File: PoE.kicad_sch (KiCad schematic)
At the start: 86 parts, among them Q2 BSZ440N10NS3GATMA1, Q3 MMBTA06, T1 PA2467NL, U23 MP8008, U24 TCMT1107, U28 TCMT1107, U29 TL431DBZ

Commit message: Weeded out all ERC errors
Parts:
- removed C95: 220u/25V, Capacitor_Tantalum_SMD:CP_EIA-7343-31_Kemet-D, symbol Device:CP_Small
- added R903: 51R, Resistor_SMD:R_0402_1005Metric, symbol Device:R_Small
- added R906: 75R, Resistor_SMD:R_0402_1005Metric, symbol Device:R_Small
- added R916, R917: 24k, Resistor_SMD:R_0805_2012Metric, symbol Device:R_Small
- C901: renamed from C75; value 220n/50V -> 220nF/50V; LCSC (none) -> C5378
- C902: renamed from C16; value 10n/100V -> 10nF/100V; LCSC (none) -> C24944
- C903: renamed from C83; value 10n/100V -> 10nF/100V; LCSC (none) -> C24944
- C904: renamed from C110; value 10n/100V -> 10nF/100V; LCSC (none) -> C24944
- C905: renamed from C74; value 10n/100V -> 10nF/100V; LCSC (none) -> C24944
- C906: renamed from C76; value 1n/100V -> 1nF/100V; LCSC (none) -> C28233
- C907: renamed from C73; value 4u7/16V -> 4.7uF/16V; LCSC (none) -> C1779
- C908: renamed from C89; value 2u2/100V -> 2.2uF/100V; LCSC (none) -> C7393990
- C909: renamed from C79; value 100n/100V -> 100nF/100V; LCSC (none) -> C28233
- C910: renamed from C82; value 100n/100V -> 100nF/100V; LCSC (none) -> C28233
- C911: renamed from C84; value 100n/100V -> 100nF/100V; LCSC (none) -> C28233
- C912: renamed from C85; value 47u/63V -> 47uF/63V; symbol Device:CP_Small -> Device:C_Polarized_Small; LCSC (none) -> C40078
- C913: renamed from C86; value 2u2/25V -> 2.2uF/25V; LCSC (none) -> C377773
- C914: renamed from C87; value 2u2/100V -> 2.2uF/100V; LCSC (none) -> C7393990
- C915: renamed from C91; value 2u2/100V -> 2.2uF/100V; LCSC (none) -> C7393990
- C916: renamed from C92; value 220n/100V -> 220nF/100V; LCSC (none) -> C967578
- C917: renamed from C116; value 2u2/100V -> 2.2uF/100V; LCSC (none) -> C7393990
- C918: renamed from C114; LCSC (none) -> C36077
- C919: renamed from C115; LCSC (none) -> C36077
- C920: renamed from C90; LCSC (none) -> C36077
- C921: renamed from C93; LCSC (none) -> C36077
- C922: renamed from C94; value 1n/100V -> 1nF/100V; LCSC (none) -> C28233
- C923: renamed from C102; value 22u/25V -> 22uF/25V; LCSC (none) -> C45783
- C924: renamed from C77; value 100n/25V -> 100nF/25V; LCSC (none) -> C307331
- C925: renamed from C78; value 220p/25V -> 220pF/25V; LCSC (none) -> C1530
- C926: renamed from C99; value 22u/25V -> 22uF/25V; LCSC (none) -> C45783
- C927: renamed from C96; value 1u/25V -> 1uF/25V; LCSC (none) -> C52923
- C928: renamed from C105; value 22u/25V -> 22uF/25V; LCSC (none) -> C45783
- C929: renamed from C101; value 22u/25V -> 22uF/25V; LCSC (none) -> C45783
- C930: renamed from C103; value 22u/25V -> 22uF/25V; LCSC (none) -> C45783
- C931: renamed from C104; value 22u/25V -> 22uF/25V; LCSC (none) -> C45783
- C932: renamed from C80; value 680p -> 1nF; LCSC (none) -> C1523
- C933: renamed from C106; value 22u/25V -> 22uF/25V; LCSC (none) -> C45783
- D901: renamed from D19; LCSC (none) -> C21546
- D902: renamed from D10; value B1100-13-F -> SS210; LCSC (none) -> C14996
- D903: renamed from D11; value B1100-13-F -> SS210; LCSC (none) -> C14996
- D904: renamed from D12; value B1100-13-F -> SS210; LCSC (none) -> C14996
- D905: renamed from D13; value B1100-13-F -> SS210; LCSC (none) -> C14996
- D906: renamed from D14; value B1100-13-F -> SS210; LCSC (none) -> C14996
- D907: renamed from D15; value B1100-13-F -> SS210; LCSC (none) -> C14996
- D908: renamed from D16; value B1100-13-F -> SS210; LCSC (none) -> C14996
- D909: renamed from D17; value B1100-13-F -> SS210; LCSC (none) -> C14996
- D910: renamed from D18; value SMBJ58A-13-F -> SMBJ58A; LCSC (none) -> C41376102; Manufacturer Diodes Incorporated -> (none); PartNumber SMBJ58A-13-F -> (none)
- D911: renamed from D20; value BAT41ZFILM -> BAT46W; LCSC (none) -> C7420332
- D912: renamed from D21; value BAT41ZFILM -> BAT46W; LCSC (none) -> C7420332
- D913: renamed from D22; value MMSD4448 -> SM4007PL; LCSC (none) -> C64898; Manufacturer ON Semiconductor -> (none); PartNumber MMSD4448 -> BAT46W
- D914: renamed from D23; value B340LB-13-F -> SS510B; LCSC (none) -> C7420368
- FB901: renamed from FB2; footprint Resistor_SMD:R_0805_2012Metric -> Inductor_SMD:L_0805_2012Metric; symbol Device:Ferrite_Bead_Small -> Device:FerriteBead_Small; LCSC (none) -> C44838; Manufacturer Würth Elektronik -> (none); PartNumber 742792031 -> (none)
- FB902: renamed from FB3; footprint Resistor_SMD:R_0805_2012Metric -> Inductor_SMD:L_0805_2012Metric; symbol Device:Ferrite_Bead_Small -> Device:FerriteBead_Small; LCSC (none) -> C44838
- FL901: renamed from FL1; footprint Yellow:L_CommonModeChoke_Murata_DLW5B -> Hatlabs:L_CommonModeChoke_Sunltech_SMW5045S102LTT; LCSC (none) -> C254911; Manufacturer Murata Electronics -> (none); PartNumber DLW5BTM102SQ2 -> (none)
- JP901: renamed from JP5; LCSC (none) -> C49257
- L901: renamed from L4; value 10u -> 10uH; footprint Inductor_SMD:L_Taiyo-Yuden_NR-50xx -> Inductor_SMD:L_Changjiang_FXL0630; LCSC (none) -> C167223; Manufacturer Taiyo Yuden -> cjiang; PartNumber NRS5040T100MMGJV -> FXL0630-100-M
- L902: renamed from L5; value 2u2 -> 2.2uH; footprint Inductor_SMD:L_Taiyo-Yuden_NR-50xx -> Inductor_SMD:L_Changjiang_FXL0530; LCSC (none) -> C177247; Manufacturer Taiyo Yuden -> cjiang; PartNumber NRS5040T2R2NMGJ -> FXL0530-2R2-M
- Q901: renamed from Q3; value MMBTA06 -> MMBT5551; LCSC (none) -> C2145; Manufacturer Diodes Incorporated -> (none); PartNumber MMBTA06-7-F -> (none)
- Q902: renamed from Q2; value BSZ440N10NS3GATMA1 -> CSD19538Q3A; footprint Yellow:PG-TSDSON-8 -> Package_TO_SOT_SMD:TDSON-8-1; LCSC (none) -> C478471; Manufacturer Infineon Technologies -> Texas Instruments; PartNumber BSZ440N10NS3GATMA1 -> CSD19538Q3A
- R901: renamed from R10; value 49k9 -> 49.9k; LCSC (none) -> C25897
- R902: renamed from R12; LCSC (none) -> C11702
- R904: renamed from R24; value 41R2/1% -> 220R; LCSC (none) -> C25091
- R905: renamed from R42; value 28R7/1% -> 47R; LCSC (none) -> C25118
- R907: renamed from R45; value 49k9 -> 49.9k; LCSC (none) -> C25897
- R908: renamed from R19; value 24k9/1% -> 24.9k; LCSC (none) -> C25874
- R909: renamed from R46; LCSC (none) -> C25768
- R910: renamed from R43; LCSC (none) -> C25744
- R911: renamed from R57; LCSC (none) -> C17561
- R912: renamed from R56; value 3k3 -> 3.3k; LCSC (none) -> C25890
- R913: renamed from R58; value 4k99 -> 4.99k; footprint Resistor_SMD:R_0402_1005Metric -> Resistor_SMD:R_0603_1608Metric; LCSC (none) -> C23046
- R914: renamed from R60; value 0R05/1% -> 50m; LCSC (none) -> C5159739
- R915: renamed from R59; value 4R7 -> 4.7R; LCSC (none) -> C17675
- R918: renamed from R47; LCSC (none) -> C11702
- R919: renamed from R63; value 12k -> 24k; footprint Resistor_SMD:R_1206_3216Metric -> Resistor_SMD:R_0805_2012Metric; LCSC (none) -> C17575
- R920: renamed from R15; value 12k -> 24k; footprint Resistor_SMD:R_1206_3216Metric -> Resistor_SMD:R_0805_2012Metric; LCSC (none) -> C17575
- R921: renamed from R64; LCSC (none) -> C17633
- R922: renamed from R48; LCSC (none) -> C4109
- R923: renamed from R44; value 3k3 -> 3.3k; LCSC (none) -> C26010
- R924: renamed from R49; value 6k8 -> 6.8k; LCSC (none) -> C25917
- R925: renamed from R65; LCSC (none) -> C17408
- R926: renamed from R50; value 49k9 -> 49.9k; LCSC (none) -> C25897
- R927: renamed from R51; LCSC (none) -> C25077
- R928: renamed from R52; value 191k -> 150k; footprint Resistor_SMD:R_0402_1005Metric -> Resistor_SMD:R_0603_1608Metric; LCSC (none) -> C22807
- R929: renamed from R53; value 49k9 -> 49.9k; footprint Resistor_SMD:R_0402_1005Metric -> Resistor_SMD:R_0603_1608Metric; LCSC (none) -> C23184
- T901: renamed from T1; LCSC (none) -> C6626468
- U901: renamed from U23; symbol Yellow:MP8008 -> Hatlabs:MP8008
- U902: renamed from U24; LCSC (none) -> C81148
- U903: renamed from U28; LCSC (none) -> C81148
- U904: renamed from U29; LCSC (none) -> C181103
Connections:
- net GNDS: now also R903.1, R906.1
- net N1B: now also R916.1, R917.1
- net at C916.1, D913.1 (K), R919.2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: now also R916.2, R917.2
- net at JP901.1 (A), R905.2: now also R906.2
- net at JP901.3 (B), R904.2: now also R903.2
- net +12V renamed Vcap
- net DC_IN_F renamed Vin_prot
- net GND1 renamed GND_POE
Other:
- note added: "U902 is used to disable PoE when another DC source is active."
- note added: "VIN startup voltage regulator"
- note added: "We're feeding supercaps; large output bulk capacitance removed as redundant."
- company: Nabu Casa -> Hat Labs Oy
- title: Power over Ethernet -> HALPI2
- moved on the sheet: C901, C902, C903, C904, C905, C906, C907, C909, C916, C920, C923, C926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

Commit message: Implement ideal diodes for input and LDO power ORing
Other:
- note added: "Disable PoE when another DC source is active."
- note removed: "U902 is used to disable PoE when another DC source is active."
- moved on the sheet: C901, C907, D912, Q902, R907, R908, R909, R910, R911, R913, R914, U901

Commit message: Re-annotate schematics
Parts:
- renumbered C902 to C901, C903 to C902, C901 to C903, C908 to C907, C907 to C908, D912 to D911, D911 to D912, R913 to R912, R912 to R913

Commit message: Sprinkle test points on the schematics
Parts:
- added TP901, TP902, TP903, TP904, TP905, TP906, TP907, TP908: TestPoint, TestPoint:TestPoint_Pad_D1.0mm, symbol Connector:TestPoint
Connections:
- net CLASS: now also TP905.1
- net COMP: now also TP902.1
- net ISENSE: now also TP906.1
- net N1A: now also TP908.1
- net POE_12V: now also TP901.1
- net POE_EN: now also TP903.1
- net POE_GATE: now also TP904.1, TP907.1

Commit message: Finish component selection for USB3 hub
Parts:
- U901: LCSC (none) -> C6314883
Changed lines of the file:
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@@
+			)
+		)
+		(property "LCSC" "C6314883"
+			(at 105.41 138.43 0)
+			(effects
+				(font
+					(size 1.27 1.27)
+				)
+				(hide yes)
 			)
 		)

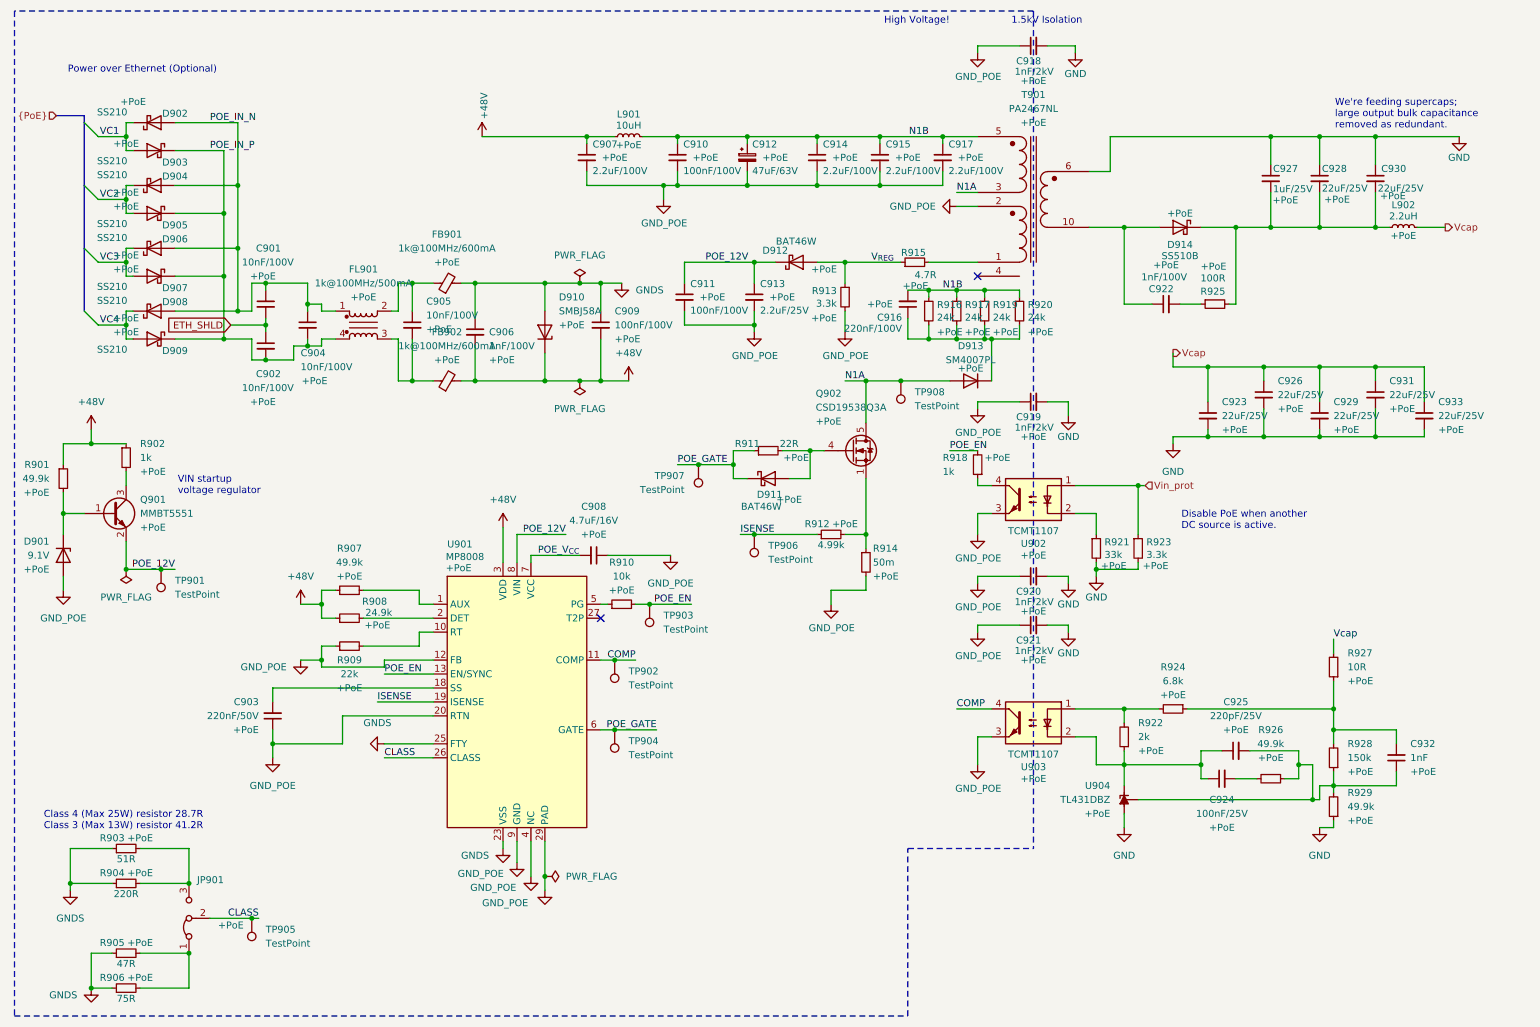
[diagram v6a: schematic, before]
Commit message: Partial trace layout, kick-ass custom rules
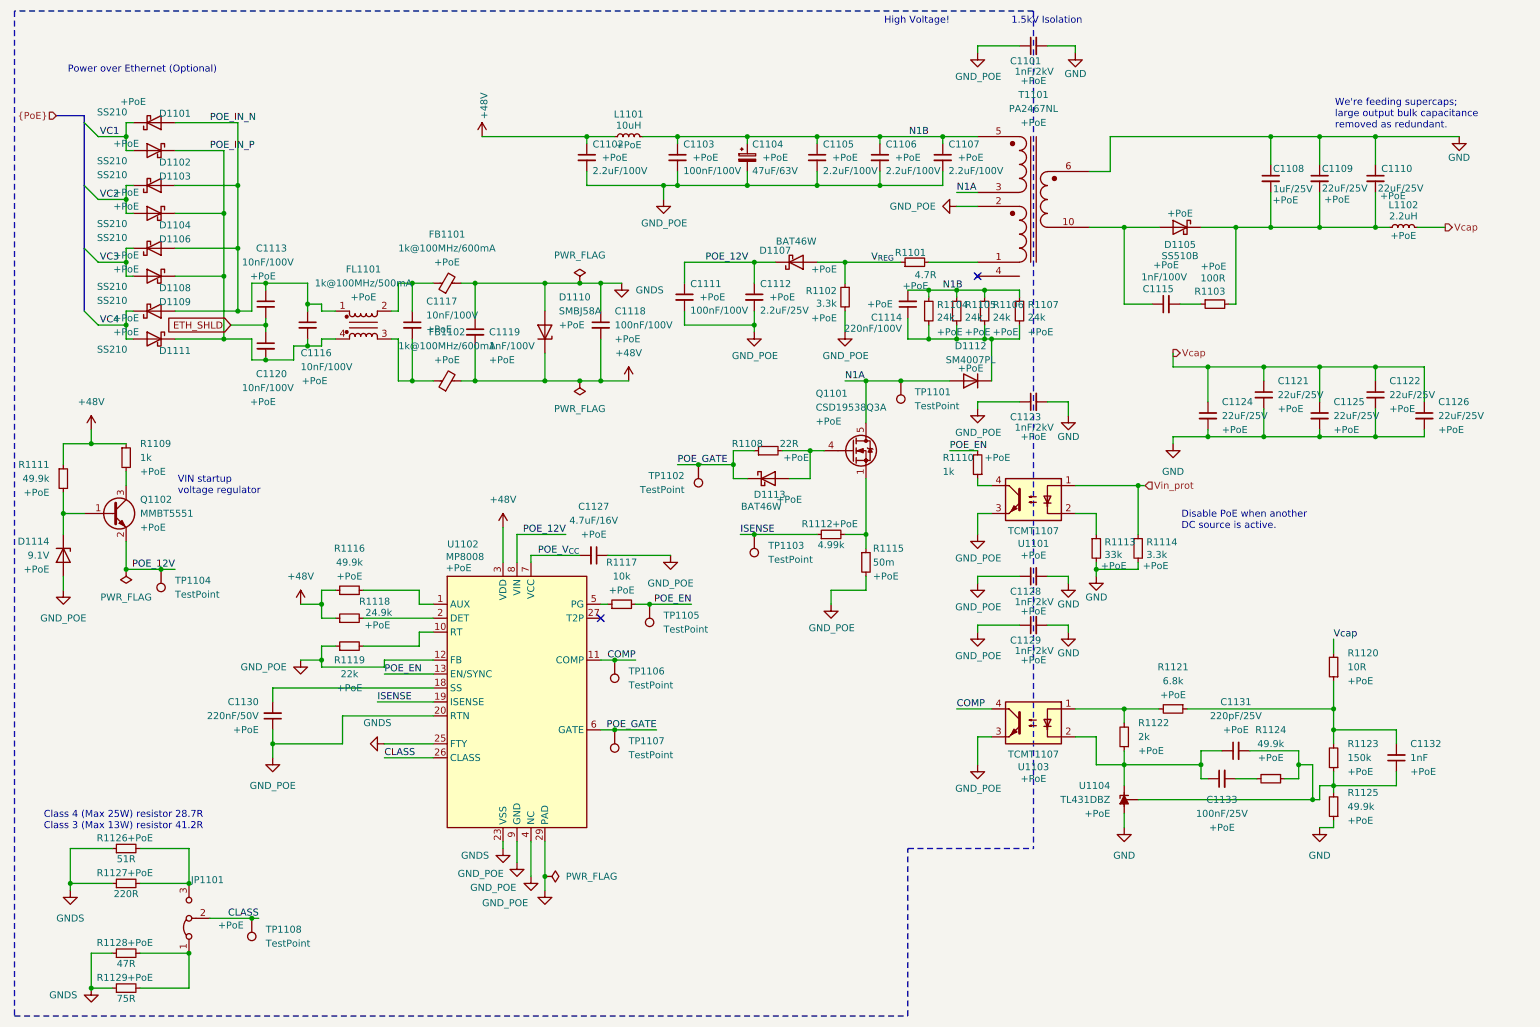
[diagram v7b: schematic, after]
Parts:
- T1101: renamed from T901; symbol Yellow:Transformer_Pulse_PA2476NL -> Hatlabs:Transformer_Pulse_PA2476NL
- renumbered C918 to C1101, C907 to C1102, C910 to C1103, C912 to C1104, C914 to C1105, C915 to C1106, C917 to C1107, C927 to C1108, C928 to C1109, C930 to C1110, C911 to C1111, C913 to C1112, C901 to C1113, C916 to C1114, C922 to C1115, C904 to C1116, C905 to C1117, C909 to C1118, C906 to C1119, C902 to C1120, C926 to C1121, C931 to C1122, C919 to C1123, C923 to C1124, C929 to C1125, C933 to C1126, C908 to C1127, C920 to C1128, C921 to C1129, C903 to C1130, C925 to C1131, C932 to C1132, C924 to C1133, D902 to D1101, D903 to D1102, D904 to D1103, D905 to D1104, D914 to D1105, D906 to D1106, D912 to D1107, D907 to D1108, D908 to D1109, D910 to D1110, D909 to D1111, D913 to D1112, D911 to D1113, D901 to D1114, FB901 to FB1101, FB902 to FB1102, FL901 to FL1101, JP901 to JP1101, L901 to L1101, L902 to L1102, Q902 to Q1101, Q901 to Q1102, R915 to R1101, R913 to R1102, R925 to R1103, R916 to R1104, R917 to R1105, R919 to R1106, R920 to R1107, R911 to R1108, R902 to R1109, R918 to R1110, R901 to R1111, R912 to R1112, R921 to R1113, R923 to R1114, R914 to R1115, R907 to R1116, R910 to R1117, R908 to R1118, R909 to R1119, R927 to R1120, R924 to R1121, R922 to R1122, R928 to R1123, R926 to R1124, R929 to R1125, R903 to R1126, R904 to R1127, R905 to R1128, R906 to R1129, TP908 to TP1101, TP907 to TP1102, TP906 to TP1103, TP901 to TP1104, TP903 to TP1105, TP902 to TP1106, TP904 to TP1107, TP905 to TP1108, U902 to U1101, U901 to U1102, U903 to U1103, U904 to U1104
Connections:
- net at T1101.4 (NC): now also T1101.7, T1101.8, T1101.9
